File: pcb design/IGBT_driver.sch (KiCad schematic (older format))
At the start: 40 parts, among them J2 DESAT, Q13 NPN, Q14 PNP, U1 ISO5852S

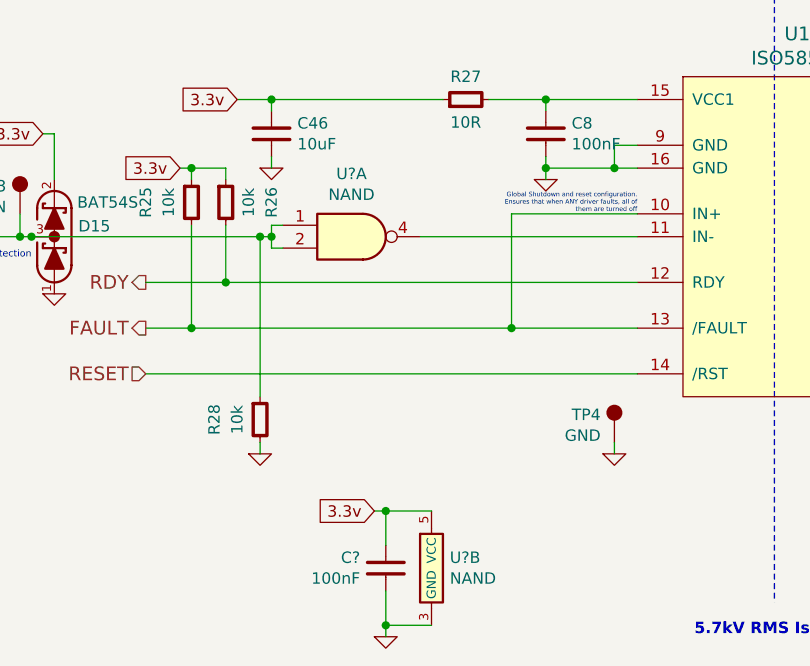
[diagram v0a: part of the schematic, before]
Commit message: Fixed schematic label and more layout
Signed-off-by: Marcos Chaparro <mchaparro@paltatech.com>
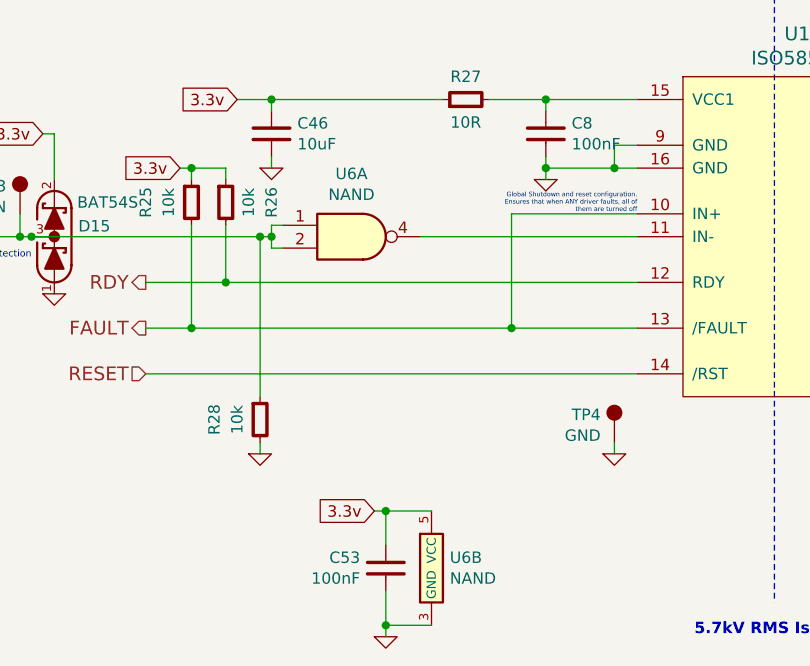
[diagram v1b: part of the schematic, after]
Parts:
- gave numbers to parts that had none: 2
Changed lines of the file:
@@
 -8V
 $Comp
-L GND #PWR04
+L GND #PWR06
 U 1 1 58241AEC
 P 3150 4050
-AR Path="/5822D62D/58241AEC" Ref="#PWR04"  Part="1"
-AR Path="/5824556D/58241AEC" Ref="#PWR021"  Part="1"
-F 0 "#PWR04" H 3150 4050 30  0001 C CNN
+AR Path="/5822D62D/58241AEC" Ref="#PWR06"  Part="1"
+AR Path="/5824556D/58241AEC" Ref="#PWR023"  Part="1"
+F 0 "#PWR06" H 3150 4050 30  0001 C CNN
 F 1 "GND" H 3150 3980 30  0001 C CNN
 F 2 "" H 3150 4050 60  0000 C CNN
@@
 $EndComp
 $Comp
-L GND #PWR05
+L GND #PWR07
 U 1 1 5830FC3F
 P 1950 4000
-AR Path="/5822D62D/5830FC3F" Ref="#PWR05"  Part="1"
-AR Path="/5824556D/5830FC3F" Ref="#PWR022"  Part="1"
-F 0 "#PWR05" H 1950 4000 30  0001 C CNN
+AR Path="/5822D62D/5830FC3F" Ref="#PWR07"  Part="1"
+AR Path="/5824556D/5830FC3F" Ref="#PWR024"  Part="1"
+F 0 "#PWR07" H 1950 4000 30  0001 C CNN
 F 1 "GND" H 1950 3930 30  0001 C CNN
 F 2 "" H 1950 4000 60  0000 C CNN
@@
 $EndComp
 $Comp
-L GND #PWR06
+L GND #PWR08
 U 1 1 58363068
 P 3450 5250
-AR Path="/5822D62D/58363068" Ref="#PWR06"  Part="1"
-AR Path="/5824556D/58363068" Ref="#PWR023"  Part="1"
-F 0 "#PWR06" H 3450 5250 30  0001 C CNN
+AR Path="/5822D62D/58363068" Ref="#PWR08"  Part="1"
+AR Path="/5824556D/58363068" Ref="#PWR025"  Part="1"
+F 0 "#PWR08" H 3450 5250 30  0001 C CNN
 F 1 "GND" H 3450 5180 30  0001 C CNN
 F 2 "" H 3450 5250 60  0000 C CNN
@@
 Connection ~ 900  4300
 $Comp
-L GND #PWR08
+L GND #PWR09
 U 1 1 583666D4
 P 1000 4550
-AR Path="/5822D62D/583666D4" Ref="#PWR08"  Part="1"
-AR Path="/5824556D/583666D4" Ref="#PWR025"  Part="1"
-F 0 "#PWR08" H 1000 4550 30  0001 C CNN
+AR Path="/5822D62D/583666D4" Ref="#PWR09"  Part="1"
+AR Path="/5824556D/583666D4" Ref="#PWR026"  Part="1"
+F 0 "#PWR09" H 1000 4550 30  0001 C CNN
 F 1 "GND" H 1000 4480 30  0001 C CNN
 F 2 "" H 1000 4550 60  0000 C CNN
@@
 $EndComp
 $Comp
-L GND #PWR09
+L GND #PWR010
 U 1 1 58368450
 P 1900 5250
-AR Path="/5822D62D/58368450" Ref="#PWR09"  Part="1"
-AR Path="/5824556D/58368450" Ref="#PWR026"  Part="1"
-F 0 "#PWR09" H 1900 5250 30  0001 C CNN
+AR Path="/5822D62D/58368450" Ref="#PWR010"  Part="1"
+AR Path="/5824556D/58368450" Ref="#PWR027"  Part="1"
+F 0 "#PWR010" H 1900 5250 30  0001 C CNN
 F 1 "GND" H 1900 5180 30  0001 C CNN
 F 2 "" H 1900 5250 60  0000 C CNN
@@
 Connection ~ 850  4300
 $Comp
-L 741G00-SOT23 U?
+L 741G00-SOT23 U6
 U 2 1 58394A62
 P 2650 5450
-AR Path="/5822D62D/58394A62" Ref="U?"  Part="2"
-AR Path="/5824556D/58394A62" Ref="U?"  Part="2"
-F 0 "U?" H 2730 5196 50  0000 L CNN
+AR Path="/5822D62D/58394A62" Ref="U6"  Part="2"
+AR Path="/5824556D/58394A62" Ref="U7"  Part="2"
+F 0 "U6" H 2730 5196 50  0000 L CNN
 F 1 "NAND" H 2730 5105 50  0000 L CNN
 F 2 "smd-semi:SOT-23-5" H 2650 5300 50  0001 C CNN
@@
 P 2350 4300
 AR Path="/58394A6A" Ref="U?"  Part="1"
-AR Path="/5822D62D/58394A6A" Ref="U?"  Part="1"
-AR Path="/5824556D/58394A6A" Ref="U?"  Part="1"
-F 0 "U?" H 2300 4575 50  0000 C CNN
+AR Path="/5822D62D/58394A6A" Ref="U6"  Part="1"
+AR Path="/5824556D/58394A6A" Ref="U7"  Part="1"
+F 0 "U6" H 2300 4575 50  0000 C CNN
 F 1 "NAND" H 2300 4484 50  0000 C CNN
 F 2 "smd-semi:SOT-23-5" H 2350 4150 50  0001 C CNN
@@
 $EndComp
 $Comp
-L C-0603 C?
+L C-0603 C53
 U 1 1 58394A72
 P 2450 5750
-AR Path="/5822D62D/58394A72" Ref="C?"  Part="1"
-AR Path="/5824556D/58394A72" Ref="C?"  Part="1"
-F 0 "C?" H 2562 5796 50  0000 L CNN
+AR Path="/5822D62D/58394A72" Ref="C53"  Part="1"
+AR Path="/5824556D/58394A72" Ref="C54"  Part="1"
+F 0 "C53" H 2562 5796 50  0000 L CNN
 F 1 "100nF" H 2562 5705 50  0000 L CNN
 F 2 "IPC7351-Nominal:CAPC1608X55" H 2450 5750 50  0001 C CNN
@@
 	2450 5850 2450 6050
 $Comp
-L GND #PWR?
+L GND #PWR011
 U 1 1 58394A7D
 P 2450 6050
-AR Path="/5822D62D/58394A7D" Ref="#PWR?"  Part="1"
-AR Path="/5824556D/58394A7D" Ref="#PWR?"  Part="1"
-F 0 "#PWR?" H 2450 6050 30  0001 C CNN
+AR Path="/5822D62D/58394A7D" Ref="#PWR011"  Part="1"
+AR Path="/5824556D/58394A7D" Ref="#PWR028"  Part="1"
+F 0 "#PWR011" H 2450 6050 30  0001 C CNN
 F 1 "GND" H 2450 5980 30  0001 C CNN
 F 2 "" H 2450 6050 60  0000 C CNN

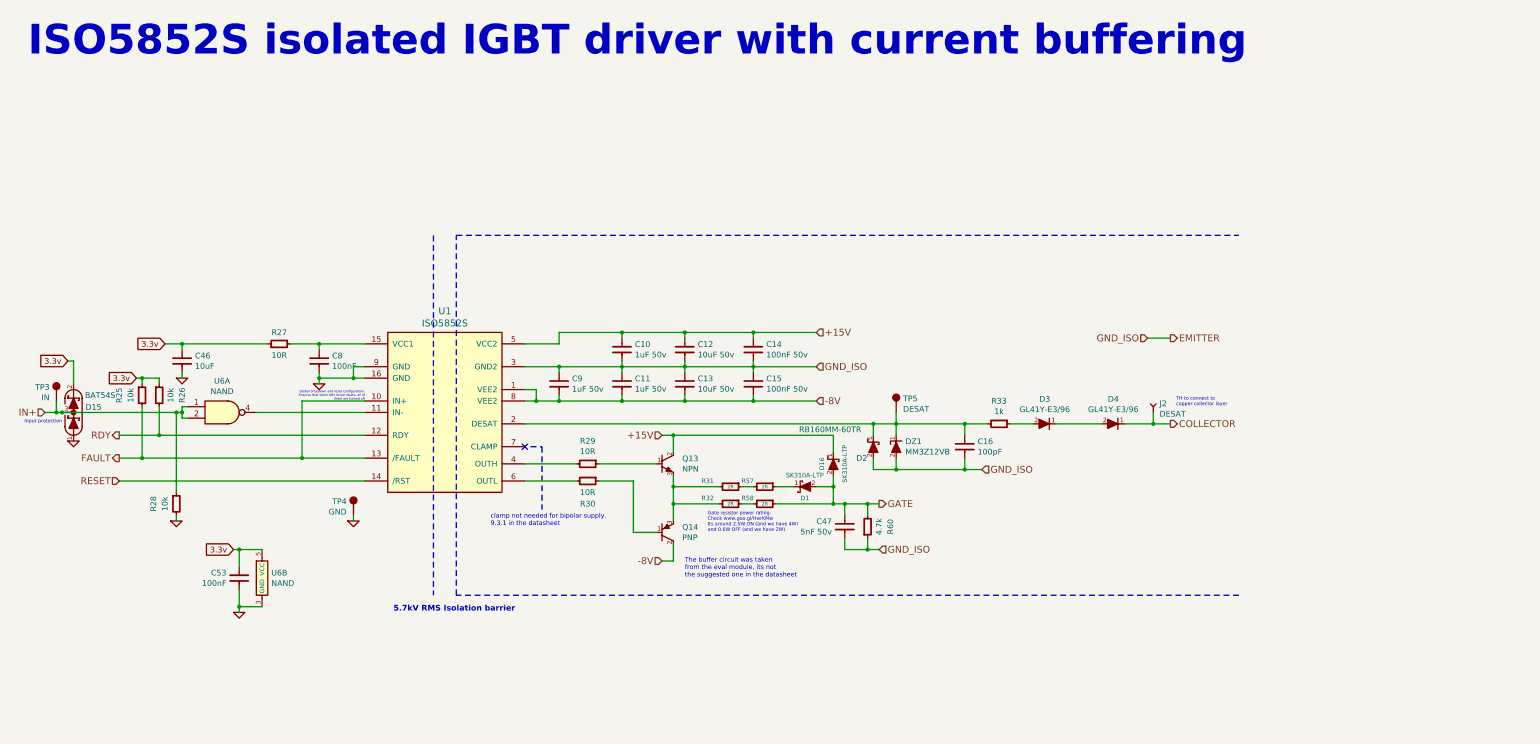
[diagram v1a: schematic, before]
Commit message: Added gate voltage control, more decoupling pads for the buffer transistors, added notes
Signed-off-by: Marcos Chaparro <mchaparro@paltatech.com>
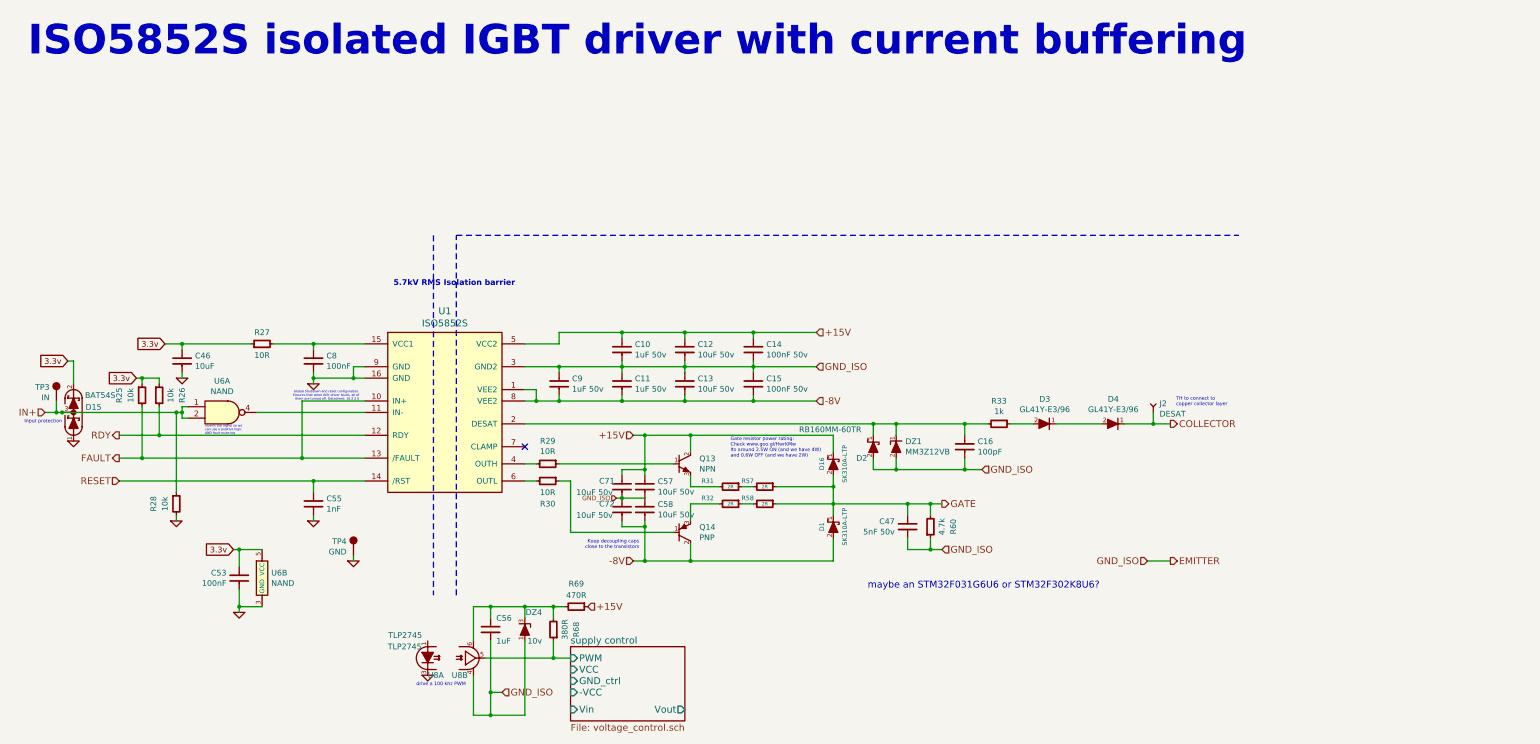
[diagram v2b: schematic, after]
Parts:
- removed TP5: DESAT, conn-test:TEST-SMD-SMALL, symbol TESTPOINT
- added C55: 1nF, IPC7351-Nominal:CAPC1608X55, symbol C-0603
- added C56: 1uF, IPC7351-Nominal:CAPC1608X55, symbol C-0603
- added C57, C58, C71, C72: 10uF 50v, IPC7351-Nominal:CAPC3216X70, symbol C-1206
- added DZ4: 10v, smd-semi:SOT-23, symbol BZX84
- added R68: 380R, IPC7351-Nominal:RESC1608X50, symbol R-0603
- added R69: 470R, IPC7351-Nominal:RESC1608X50, symbol R-0603
- added U8: TLP2745, paltatech:SDIP6, symbol TLP2745
- R31, R57: BOM RES SMD 1k 5% [2512] -> RES SMD 10R 1% 2W [2512]
- R32, R58: BOM RES SMD 1k 5% [2512] -> RES SMD 1k 1% [2512]
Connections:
- net +15V: now also C57.1, C71.1, R69.1
- net -8V: now also D1.2 (A), C58.2, C72.2
- net EMITTER: now also C56.2, C57.2, C58.1, C71.2, C72.1, DZ4.1 (A), U8.4 (GND)
- net GATE: now also D1.1 (K), R57.1; no longer D1.2 (A)
- net GND: now also C55.2, U8.3 (K)
- net RESET: now also C55.1
- net at Q13.3 (E), R31.2: no longer Q14.3 (E), R32.2
- new net: Q14.3 (E), R32.2
- new net: C56.1, DZ4.3 (K), R68.2, R69.2, U8.6 (VCC)
- new net supply control/PWM: R68.1, U8.5 (Vo)
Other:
- note added: "Global Shutdown and reset configuration.\nEnsures that when ANY driver faults, all of\nthem are turned off. Datasheet: 10.2.2.5"
- note added: "Inverts the signal so we\ncan use a positive logic\nAND fault mute-ing"
- note added: "Keep decoupling caps\nclose to the transistors"
- note added: "drive a 100 khz PWM"
- note added: "maybe an STM32F031G6U6 or STM32F302K8U6?"
- note removed: "Global Shutdown and reset configuration.\nEnsures that when ANY driver faults, all of\nthem are turned off"
- note removed: "The buffer circuit was taken\nfrom the eval module, its not\nthe suggested one in the datasheet"
- note removed: "clamp not needed for bipolar supply.\n9.3.1 in the datasheet"
- moved on the sheet: C47, C8, Q13, Q14, R27, R29, R30, R60, TP4

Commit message: Removed old comments, added notes, connected programmable -VEE
Signed-off-by: Marcos Chaparro <mchaparro@paltatech.com>
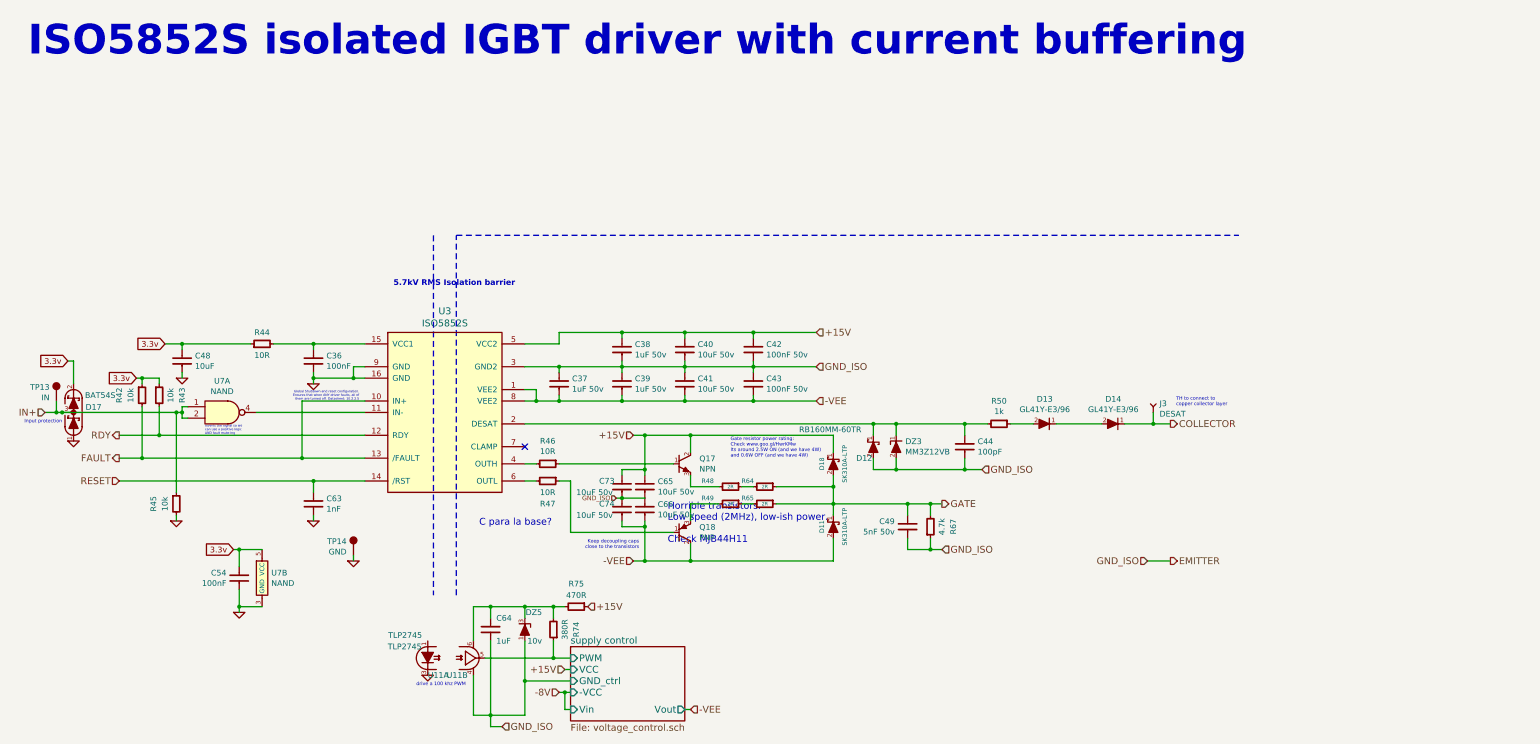
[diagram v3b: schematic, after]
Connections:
- net -8V: no longer C11.2, C13.2, C15.2, C58.2, C72.2, C9.2, D1.2 (A), Q14.2 (C), U1.1 (VEE2), U1.8 (VEE2)
- new net -VEE: C11.2, C13.2, C15.2, C58.2, C72.2, C9.2, D1.2 (A), Q14.2 (C), U1.1 (VEE2), U1.8 (VEE2)
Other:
- note added: "C para la base?"
- note added: "Gate resistor power rating:\nCheck www.goo.gl/HwrKMw\nIts around 2.5W ON (and we have 4W)\nand 0.6W OFF (and we have 4W)"
- note added: "Horrible transistors.\nLow speed (2MHz), low-ish power.\n\nCheck MJB44H11"
- note removed: "Gate resistor power rating:\nCheck www.goo.gl/HwrKMw\nIts around 2.5W ON (and we have 4W)\nand 0.6W OFF (and we have 2W)"
- note removed: "maybe an STM32F031G6U6 or STM32F302K8U6?"

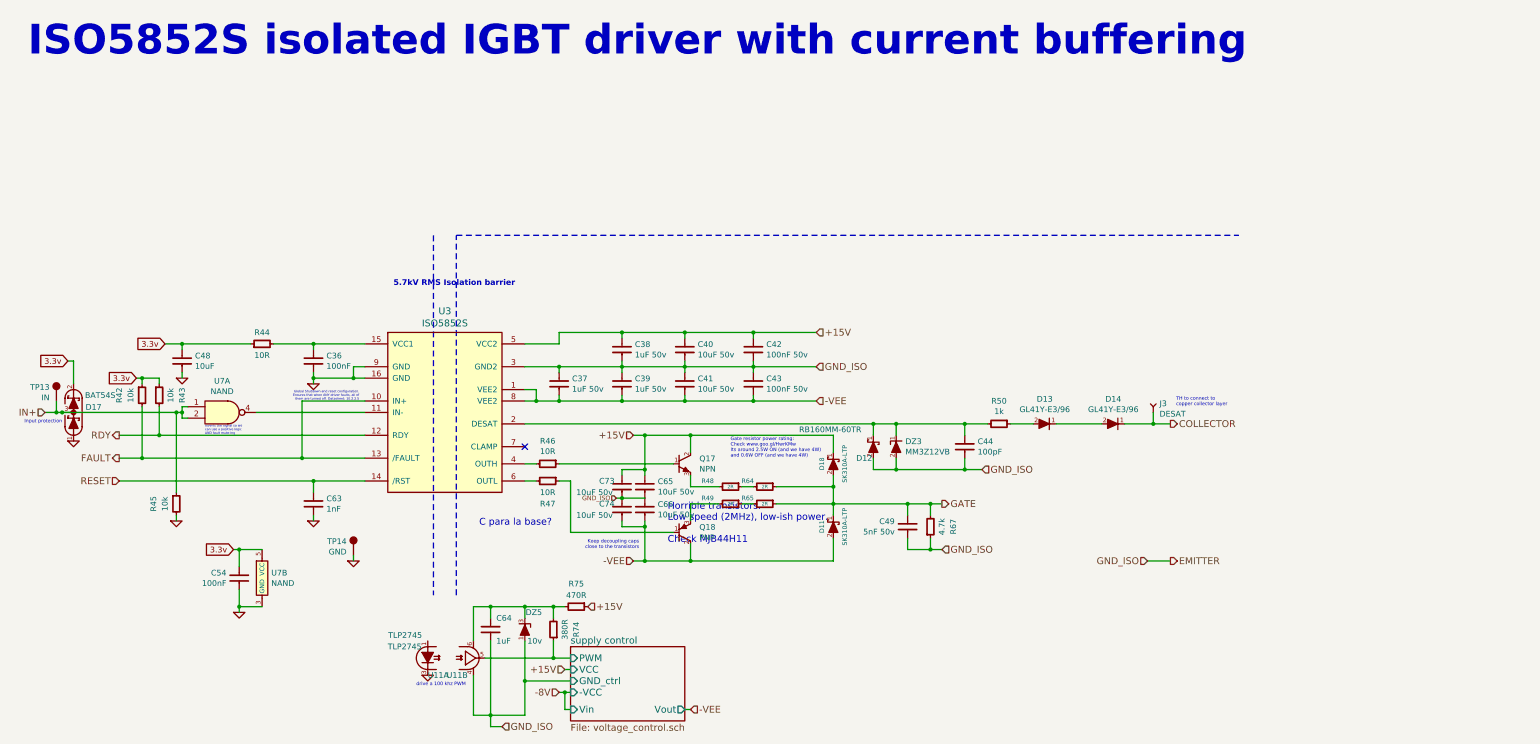
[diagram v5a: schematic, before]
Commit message: Updated gate resistor rating, qty and part#, updated desat blocking diode with much beetter recovery time
Signed-off-by: Marcos Chaparro <mchaparro@paltatech.com>
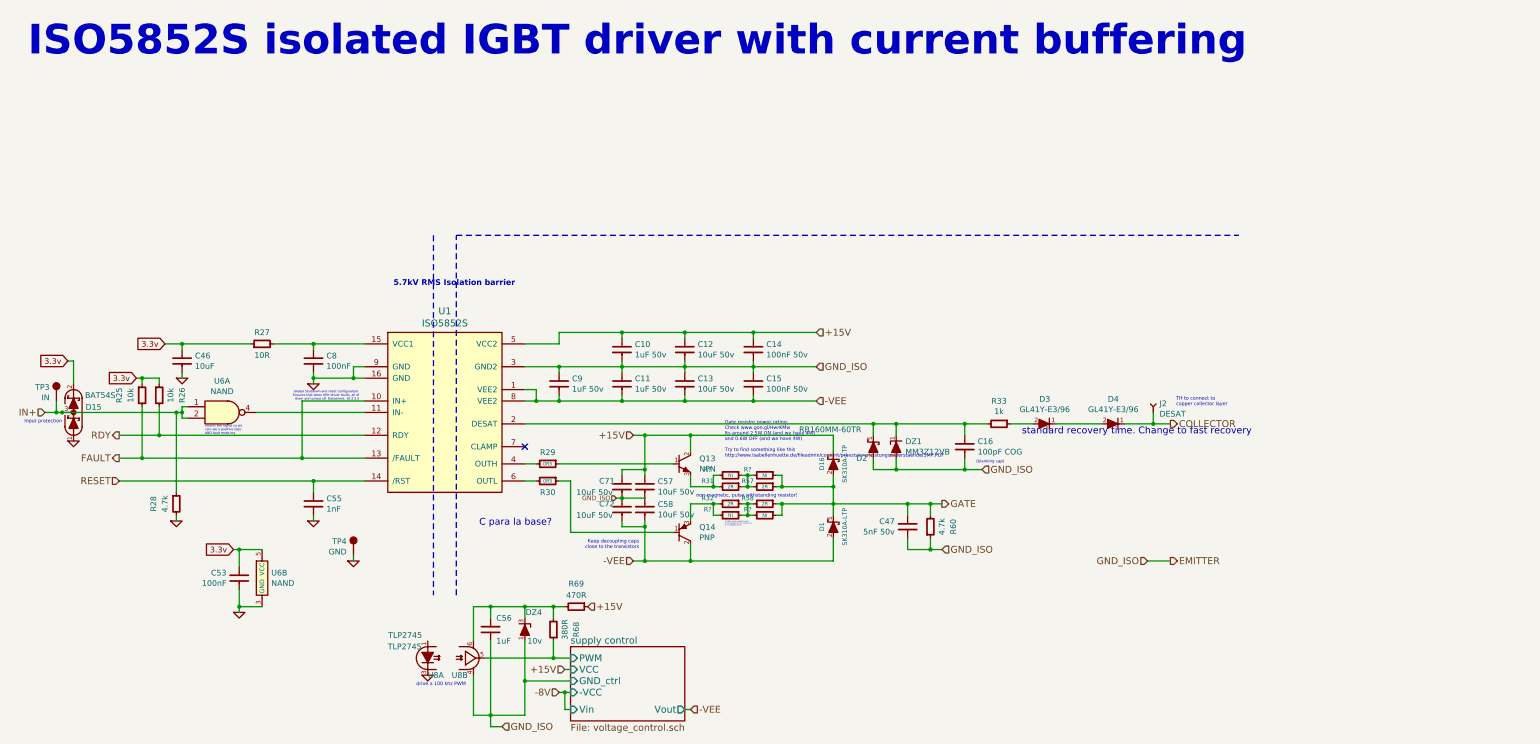
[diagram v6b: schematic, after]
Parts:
- added R? (x4): NI, IPC7351-Nominal:RESC3225X60, symbol R-0805
- C16: value 100pF -> 100pF COG
- D3, D4: footprint paltatech:melf-DO-213AB -> Diodes_SMD:Diode-SMB_Standard; #mfg (none) -> MURS160-13-F; mfg# GL41Y-E3/96 -> (none)
- R28: value 10k -> 4.7k
- R29, R30: value 10R -> 0R5
- R31, R57: #mfg (none) -> PCNM1206K2R00FST5; BOM RES SMD 10R 1% 2W [2512] -> RES SMD 2R 1% 2W +-100ppm [1206]
- R32, R58: #mfg (none) -> PCNM1206K2R00FST5; BOM RES SMD 1k 1% [2512] -> RES SMD 2R 1% 2W +-100ppm [1206]
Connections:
- net GATE: now also R?.1, R?.1
- net at Q13.3 (E), R31.2: now also R?.2
- net at Q14.3 (E), R32.2: now also R?.2
- net at R31.1, R57.2: now also R?.1, R?.2
- net at R32.1, R58.2: now also R?.1, R?.2
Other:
- note added: "(blanking cap)"
- note added: "10 Ohm vishay resistors come\nin 0.1% 25ppm for the same price\nof 1% 100ppm 2 ohm"
- note added: "Gate resistor power rating:\nCheck www.goo.gl/HwrKMw\nIts around 2.5W ON (and we have 4W)\nand 0.6W OFF (and we have 4W)\n\nTry to find something like this\nhttp://www.isabellenhuette.de/fileadmin/content/praezisions-leistungswiderstaende/SMP.PDF"
- note added: "non-magnetic, pulse withstanding resistor!"
- note added: "standard recovery time. Change to fast recovery"
- note removed: "Gate resistor power rating:\nCheck www.goo.gl/HwrKMw\nIts around 2.5W ON (and we have 4W)\nand 0.6W OFF (and we have 4W)"
- note removed: "Horrible transistors.\nLow speed (2MHz), low-ish power.\n\nCheck MJB44H11"
